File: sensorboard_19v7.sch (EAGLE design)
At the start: 105 parts, among them IC1 ECMF02-2AMX6, IC2_ESP32S2WROOMM22S2 ESP32-S2-WROOM_M22S2H3200PH3Q0, IC4 TPA6211A1DRBR, J4_USB USB_CONN, J5_AUDIO SJ-3523-SMT-TR, J6_OAT 2.5mm JACK, J7 30310-6002HB, U1 LPS22HB, U10-MAG_SENSOR MMC5983MA, U11 LDL212PV33R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

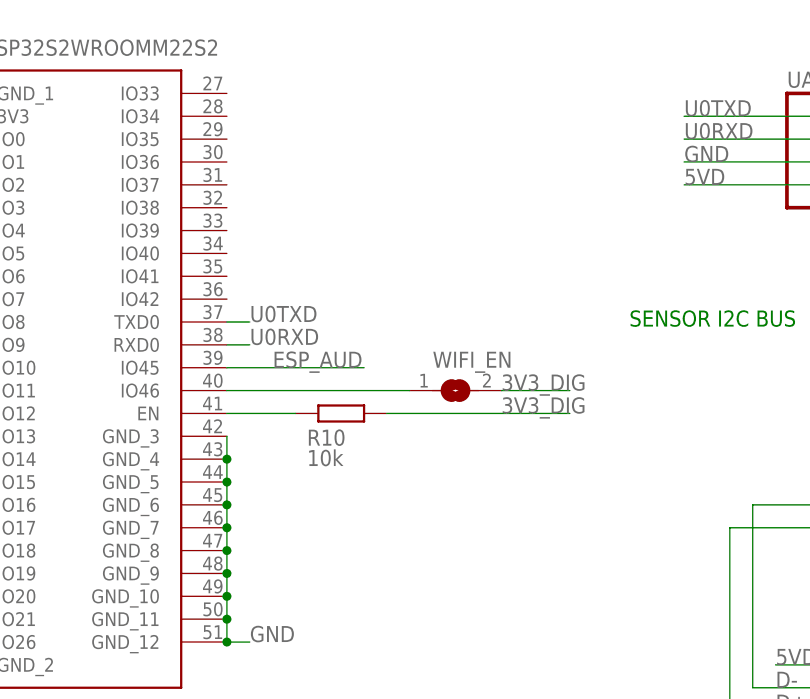
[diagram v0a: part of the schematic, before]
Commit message: Upload sensorboard_19 files
Increase via drill size
Change USB common mode filter to larger part
Add 6 pin header for SPI, 5V, GND
Add ESP32 EN pin bypass capacitor

Remove sensorboard_18 files
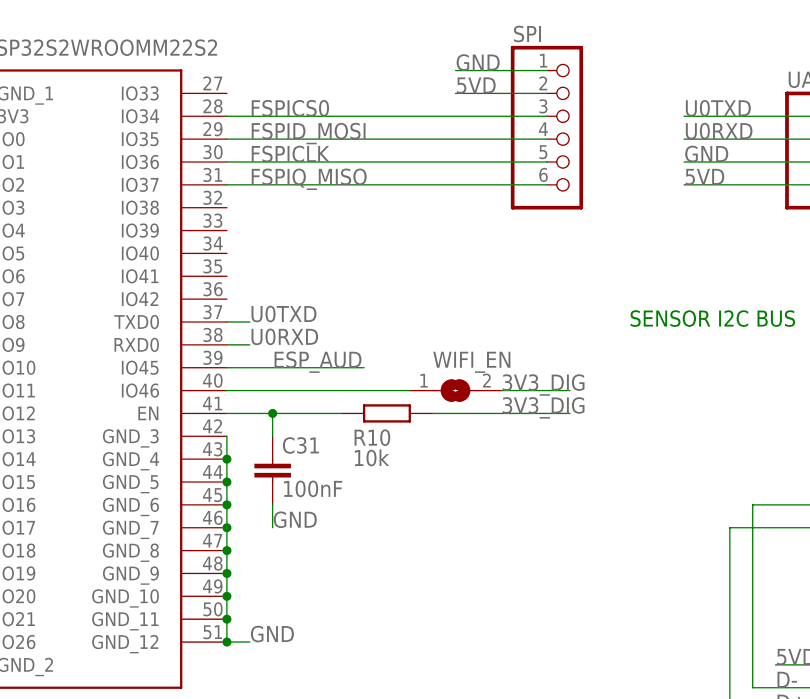
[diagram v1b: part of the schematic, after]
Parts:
- added C31: 100nF, rcl:C-EUC0603
- added SPI: (no value), pinhead_dD:PINHD-1X6
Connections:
- new net FSPICLK: IC2_ESP32S2WROOMM22S2.IO36, SPI.5
- new net FSPICS0: IC2_ESP32S2WROOMM22S2.IO34, SPI.3
- new net FSPID_MOSI: IC2_ESP32S2WROOMM22S2.IO35, SPI.4
- new net FSPIQ_MISO: IC2_ESP32S2WROOMM22S2.IO37, SPI.6
- net 5VD: now also SPI.2
- net GND: now also C31.2, SPI.1
- net N$7: now also C31.1
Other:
- moved on the sheet: R10
